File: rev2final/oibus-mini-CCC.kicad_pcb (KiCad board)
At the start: 2 copper layers, 37 x 60 mm, 91 parts, among them J1 Conn_01x04_Female, J2 USB_B_Micro, J3 uavcan_5pins, J4 Conn_01x02_Female, P1 TC2030-MCP, Q1 DMG3415U-7, Q2 NMOS, Q3 NMOS, SW1 SW_Push, SW2 SW_Push, U1 AP2112K-3.3, U10 TPD3E001DRLR, U2 SAM-M8Q, U3 NINA-B311-00B, U4 MCP73831-2-OT, U5 MCP1624T, U6 SHT31-DIS-B, U7 TCAN330, U8 STM32F303CCTx, U9 DW01C-G, Y1 16M, Y2 32kHz

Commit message: generated final rev2 assembly files ready for PCBA
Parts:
- added C13: 100n, Capacitor_SMD:C_0603_1608Metric, F.Cu at (6.10, -31.2)
- R8: value 430R -> 1k
- renumbered J4 to NFC
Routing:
- net GND: track 161.8 -> 163.6 mm
- net /on_off: track 28.8 -> 29.5 mm
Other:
- outline, holes or cut-outs redrawn

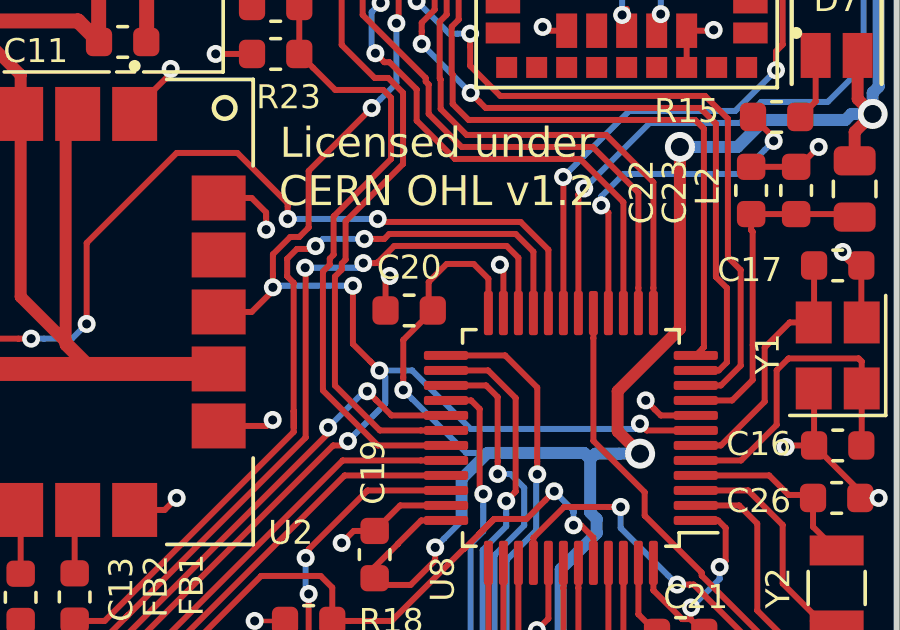
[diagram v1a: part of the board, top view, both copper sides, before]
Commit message: started generating panels
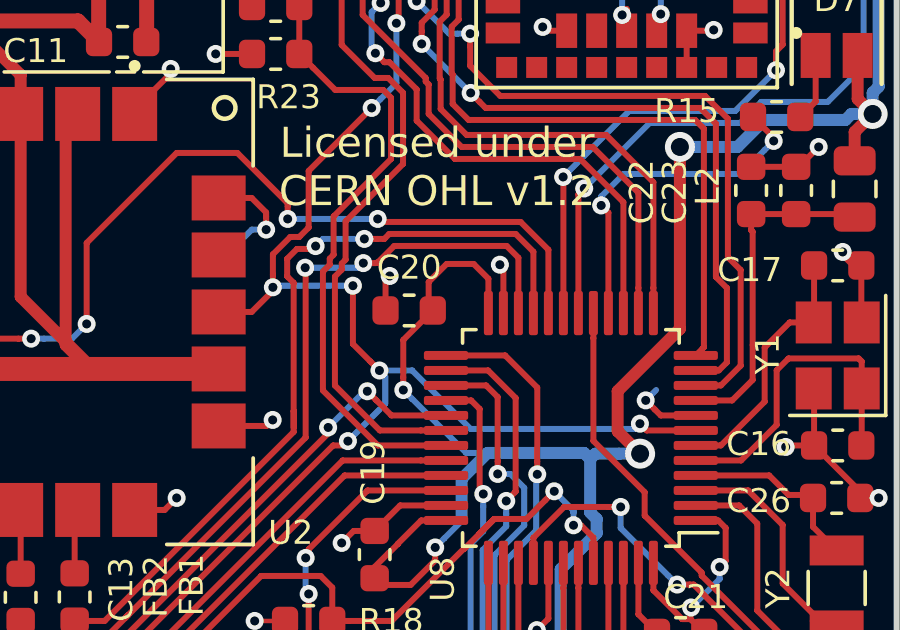
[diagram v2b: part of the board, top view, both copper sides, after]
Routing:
- net GND: track 163.6 -> 165.0 mm
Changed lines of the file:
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@@
-(kicad_pcb (version 20171130) (host pcbnew "(5.0.1-3-g963ef8bb5)")
+(kicad_pcb (version 20171130) (host pcbnew "(5.1.5-0-10_14)")
   (general
     (thickness 1.6)
     (drawings 62)
-    (tracks 1437)
+    (tracks 1440)
     (zones 0)
     (modules 92)
@@
     (zone_45_only no)
     (trace_min 0.15)
-    (segment_width 0.15)
-    (edge_width 0.15)
     (via_size 0.6)
     (via_drill 0.3)
@@
     (uvia_min_size 0.2)
     (uvia_min_drill 0.1)
+    (edge_width 0.15)
+    (segment_width 0.15)
     (pcb_text_width 0.3)
     (pcb_text_size 1.5 1.5)
@@
   (segment (start 1.393413 -17.906587) (end 2.2 -17.1) (width 0.2) (layer B.Cu) (net 2))
   (segment (start 1.393413 -21.593399) (end 1.393413 -17.906587) (width 0.2) (layer B.Cu) (net 2))
+  (segment (start 15.983313 -43.444503) (end 15.504503 -43.444503) (width 0.2) (layer B.Cu) (net 2))
+  (segment (start 15.504503 -43.444503) (end 15.24 -43.18) (width 0.2) (layer B.Cu) (net 2))
+  (segment (start 28.635285 -37.75233) (end 28.982955 -38.1) (width 0.2) (layer B.Cu) (net 2))
   (segment (start 30.269999 -26.669999) (end 28.417501 -26.669999) (width 0.2) (layer F.Cu) (net 3))
   (segment (start 30.37 -26.77) (end 30.269999 -26.669999) (width 0.2) (layer F.Cu) (net 3))
